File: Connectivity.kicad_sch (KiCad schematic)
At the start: 19 parts, among them J1 USB_C_Receptacle_USB2.0, J2 Conn_01x04_MountingPin, J3 Conn_ARM_SWD_TagConnect_TC203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, J4 2.54mm Header, Q2 Q_PMOS_GSD, U5 USBLC6-2SC6

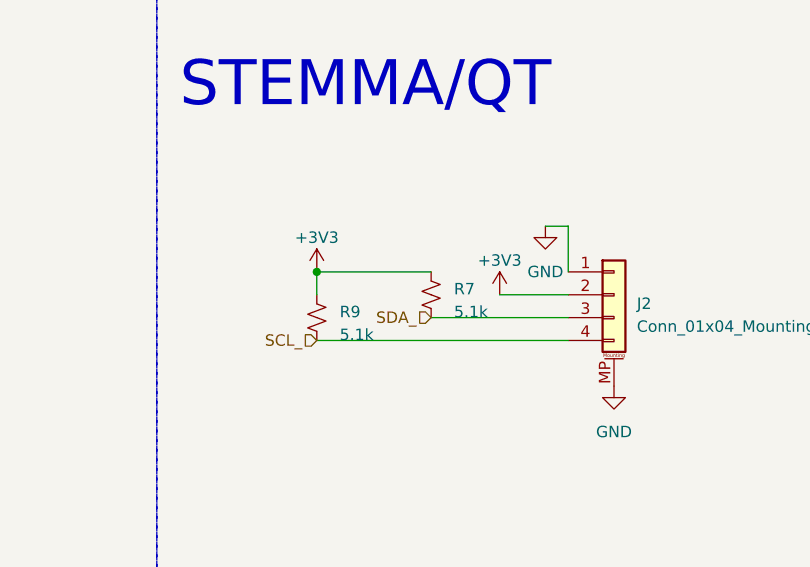
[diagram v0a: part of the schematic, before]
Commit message: Added passvies and bus connections to nRF7002
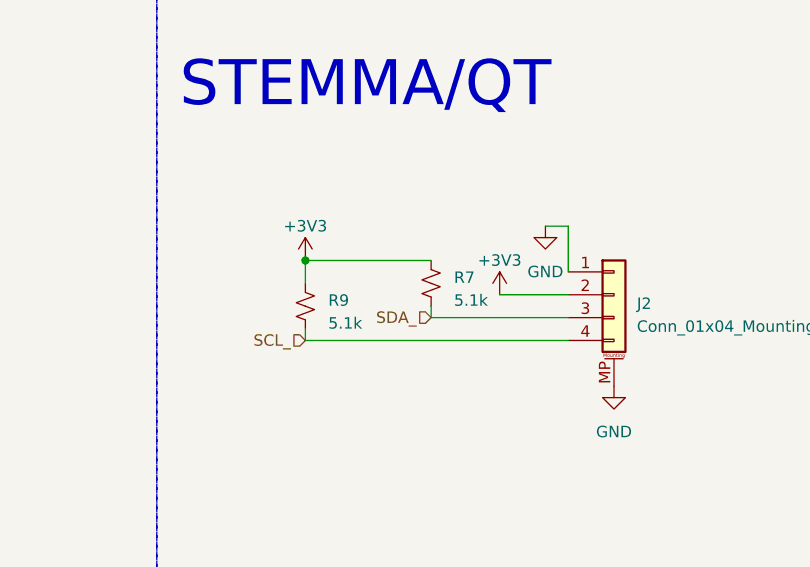
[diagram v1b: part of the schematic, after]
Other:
- moved on the sheet: R7, R9
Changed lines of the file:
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@@
   (junction (at 71.12 50.8) (diameter 0) (color 0 0 0 0)
   )
-  (junction (at 121.92 121.92) (diameter 0) (color 0 0 0 0)
+  (junction (at 120.65 120.65) (diameter 0) (color 0 0 0 0)
   )
   (junction (at 175.26 50.8) (diameter 0) (color 0 0 0 0)
@@
     (stroke (width 0) (type default))
   )
+  (wire (pts (xy 120.65 128.27) (xy 120.65 129.54))
+    (stroke (width 0) (type default))
+  )
   (wire (pts (xy 86.36 44.45) (xy 86.36 35.56))
     (stroke (width 0) (type default))
@@
     (stroke (width 0) (type default))
   )
+  (wire (pts (xy 120.65 129.54) (xy 149.86 129.54))
+    (stroke (width 0) (type default))
+  )
   (wire (pts (xy 45.72 40.64) (xy 71.12 40.64))
     (stroke (width 0) (type default))
@@
     (stroke (width 0) (type default))
   )
-  (wire (pts (xy 121.92 129.54) (xy 149.86 129.54))
-    (stroke (width 0) (type default))
-  )
   (wire (pts (xy 60.96 50.8) (xy 60.96 48.26))
     (stroke (width 0) (type default))
   )
-  (wire (pts (xy 121.92 121.92) (xy 134.62 121.92))
+  (wire (pts (xy 120.65 120.65) (xy 134.62 120.65))
     (stroke (width 0) (type default))
   )
@@
     (stroke (width 0) (type default))
   )
+  (wire (pts (xy 134.62 125.73) (xy 134.62 127))
+    (stroke (width 0) (type default))
+  )
   (wire (pts (xy 76.2 35.56) (xy 86.36 35.56))
     (stroke (width 0) (type default))
@@
     (stroke (width 0) (type default))
   )
+  (wire (pts (xy 134.62 127) (xy 149.86 127))
+    (stroke (width 0) (type default))
+  )
   (wire (pts (xy 45.72 43.18) (xy 60.96 43.18))
     (stroke (width 0) (type default))
@@
     (stroke (width 0) (type default))
   )
-  (wire (pts (xy 121.92 121.92) (xy 121.92 124.46))
+  (wire (pts (xy 120.65 120.65) (xy 120.65 123.19))
     (stroke (width 0) (type default))
   )
@@
   )
   (wire (pts (xy 93.98 35.56) (xy 93.98 44.45))
-    (stroke (width 0) (type default))
-  )
-  (wire (pts (xy 134.62 127) (xy 149.86 127))
     (stroke (width 0) (type default))
   )
@@
     (effects (font (size 1.27 1.27)) (justify right))
   )
-  (hierarchical_label "SCL_" (shape input) (at 121.92 129.54 180) (fields_autoplaced)
+  (hierarchical_label "SCL_" (shape input) (at 120.65 129.54 180) (fields_autoplaced)
     (effects (font (size 1.27 1.27)) (justify right))
   )
@@
     )
   )
-  (symbol (lib_id "Device:R_Small_US") (at 134.62 124.46 0) (unit 1)
-    (in_bom yes) (on_board yes) (dnp no) (fields_autoplaced)
-    (property "Reference" "R7" (at 137.16 123.825 0)
-      (effects (font (size 1.27 1.27)) (justify left))
-    )
-    (property "Value" "5.1k" (at 137.16 126.365 0)
-      (effects (font (size 1.27 1.27)) (justify left))
-    )
-    (property "Footprint" "" (at 134.62 124.46 0)
-      (effects (font (size 1.27 1.27)) hide)
-    )
-    (property "Datasheet" "~" (at 134.62 124.46 0)
+  (symbol (lib_id "Device:R_Small_US") (at 134.62 123.19 0) (unit 1)
+    (in_bom yes) (on_board yes) (dnp no) (fields_autoplaced)
+    (property "Reference" "R7" (at 137.16 122.555 0)
+      (effects (font (size 1.27 1.27)) (justify left))
+    )
+    (property "Value" "5.1k" (at 137.16 125.095 0)
+      (effects (font (size 1.27 1.27)) (justify left))
+    )
+    (property "Footprint" "" (at 134.62 123.19 0)
+      (effects (font (size 1.27 1.27)) hide)
+    )
+    (property "Datasheet" "~" (at 134.62 123.19 0)
       (effects (font (size 1.27 1.27)) hide)
     )
@@
     )
   )
-  (symbol (lib_id "Device:R_Small_US") (at 121.92 127 0) (unit 1)
-    (in_bom yes) (on_board yes) (dnp no) (fields_autoplaced)
-    (property "Reference" "R9" (at 124.46 126.365 0)
-      (effects (font (size 1.27 1.27)) (justify left))
-    )
-    (property "Value" "5.1k" (at 124.46 128.905 0)
-      (effects (font (size 1.27 1.27)) (justify left))
-    )
-    (property "Footprint" "" (at 121.92 127 0)
-      (effects (font (size 1.27 1.27)) hide)
-    )
-    (property "Datasheet" "~" (at 121.92 127 0)
+  (symbol (lib_id "Device:R_Small_US") (at 120.65 125.73 0) (unit 1)
+    (in_bom yes) (on_board yes) (dnp no) (fields_autoplaced)
+    (property "Reference" "R9" (at 123.19 125.095 0)
+      (effects (font (size 1.27 1.27)) (justify left))
+    )
+    (property "Value" "5.1k" (at 123.19 127.635 0)
+      (effects (font (size 1.27 1.27)) (justify left))
+    )
+    (property "Footprint" "" (at 120.65 125.73 0)
+      (effects (font (size 1.27 1.27)) hide)
+    )
+    (property "Datasheet" "~" (at 120.65 125.73 0)
       (effects (font (size 1.27 1.27)) hide)
     )
@@
     )
   )
-  (symbol (lib_id "power:+3V3") (at 121.92 121.92 0) (unit 1)
+  (symbol (lib_id "power:+3V3") (at 120.65 120.65 0) (unit 1)
     (in_bom yes) (on_board yes) (dnp no)
-    (property "Reference" "#PWR036" (at 121.92 125.73 0)
-      (effects (font (size 1.27 1.27)) hide)
-    )
-    (property "Value" "+3V3" (at 121.92 118.11 0)
-      (effects (font (size 1.27 1.27)))
-    )
-    (property "Footprint" "" (at 121.92 121.92 0)
-      (effects (font (size 1.27 1.27)) hide)
-    )
-    (property "Datasheet" "" (at 121.92 121.92 0)
-      (effects (font (size 1.27 1.27)) hide)
-    )
+    (property "Reference" "#PWR036" (at 120.65 124.46 0)
+      (effects (font (size 1.27 1.27)) hide)
+    )
+    (property "Value" "+3V3" (at 120.65 116.84 0)
+      (effects (font (size 1.27 1.27)))
+    )
+    (property "Footprint" "" (at 120.65 120.65 0)
+      (effects (font (size 1.27 1.27)) hide)
+    )
+    (property "Datasheet" "" (at 120.65 120.65 0)
+      (effects (font (size 1.27 1.27)) hide)
+    )

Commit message: Schematic complete.
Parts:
- removed R5, R6, R7, R9: 5.1k, symbol Device:R_Small_US
- D3: footprint (none) -> LED_SMD:LED_0805_2012Metric
- F1: value Polyfuse_Small -> 1A PTC; footprint (none) -> Fuse:Fuse_0402_1005Metric
- FB1: footprint (none) -> Inductor_SMD:L_0402_1005Metric; MPN (none) -> BLM15EX221SN1D
- Q2: footprint (none) -> Package_TO_SOT_SMD:SOT-323_SC-70; MPN (none) -> DMG1012UW-7
- R8: footprint (none) -> Resistor_SMD:R_0805_2012Metric
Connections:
- net D+: now also U5.1 (I/O1), U5.6 (I/O1); no longer U5.3 (I/O2), U5.4 (I/O2)
- net D-: now also U5.3 (I/O2), U5.4 (I/O2); no longer U5.1 (I/O1), U5.6 (I/O1)
- net CC2: now reaches J1.B5 (CC2)
- net CC1: now reaches J1.A5 (CC1)
- net SCL_ renamed STEMMA_SCL
- net SDA_ renamed STEMMA_SDA
- net SOC_SWO: no longer names the net of J3.6 (SWO)
- no-connect marks 3 -> 4
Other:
- moved on the sheet: BT1, D3, F1, J2, J4, JP1, Q2, R8
